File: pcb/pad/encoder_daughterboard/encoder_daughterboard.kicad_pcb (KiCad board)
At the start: 2 copper layers, 70 x 21 mm, 9 parts, among them J1 AFA07-S12FCA-00, SW1 EC11E09244BS, SW2 EC11E09244BS, SW3 EC11E09244BS

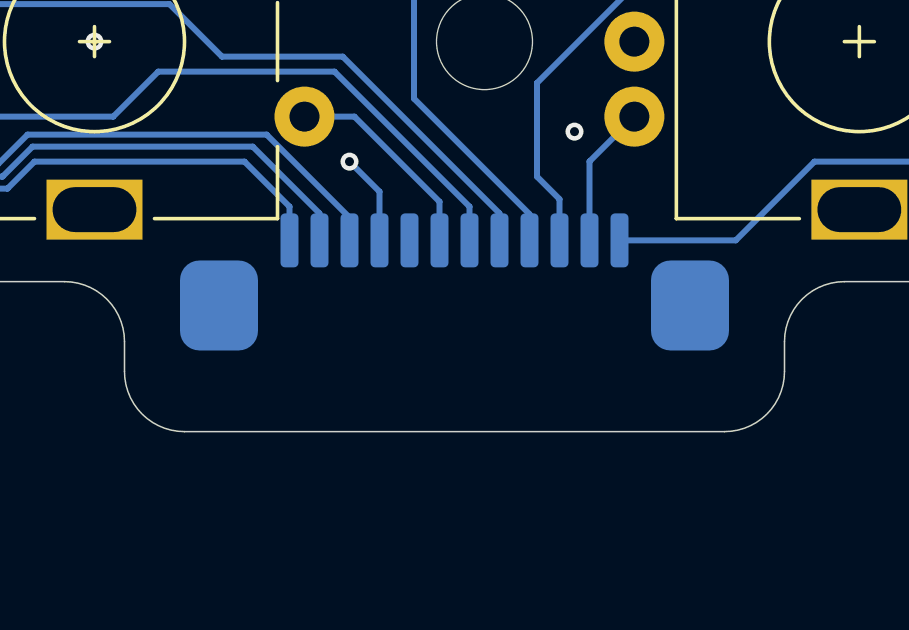
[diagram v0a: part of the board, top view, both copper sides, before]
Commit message: Update FPC connectors
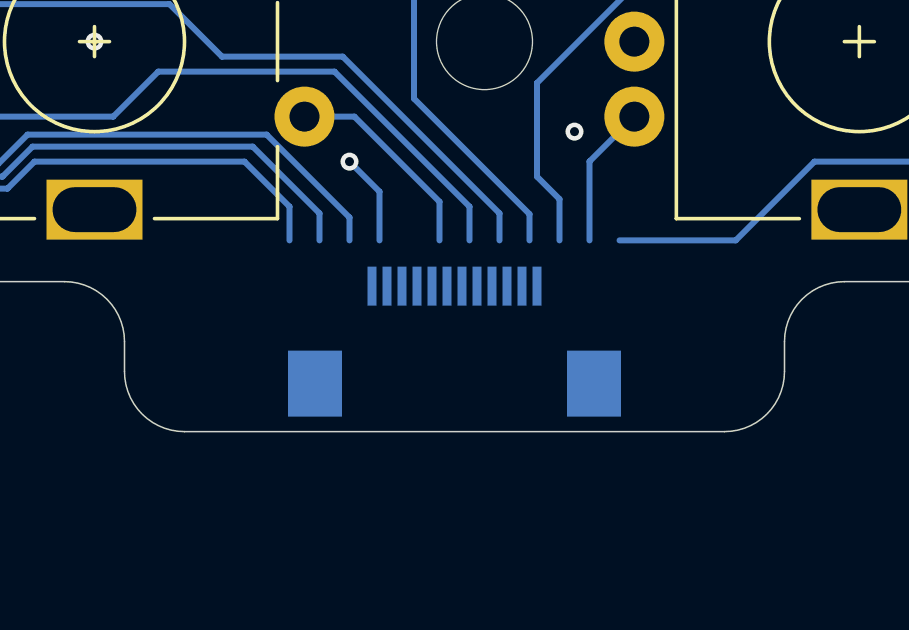
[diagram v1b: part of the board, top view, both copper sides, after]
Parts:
- J1: footprint Connector_FFC-FPC:JUSHUO_AFA07-S12FCA-00_1x12-1MP_P1.0mm_Horizontal -> Connector_FFC-FPC:Hirose_FH12-12S-0.5SH_1x12-1MP_P0.50mm_Horizontal
